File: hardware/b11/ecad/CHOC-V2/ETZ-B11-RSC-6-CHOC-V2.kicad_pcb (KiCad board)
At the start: 2 copper layers, 131.5 x 85.8 mm, 44 parts, among them SW1 Kailh_socket_PG1350, SW10 Kailh_socket_PG1350, SW11 Kailh_socket_PG1350, SW12 Kailh_socket_PG1350, SW13 Kailh_socket_PG1350, SW14 Kailh_socket_PG1350, SW15 Kailh_socket_PG1350, SW16 Kailh_socket_PG1350, SW17 Kailh_socket_PG1350, SW18 Kailh_socket_PG1350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

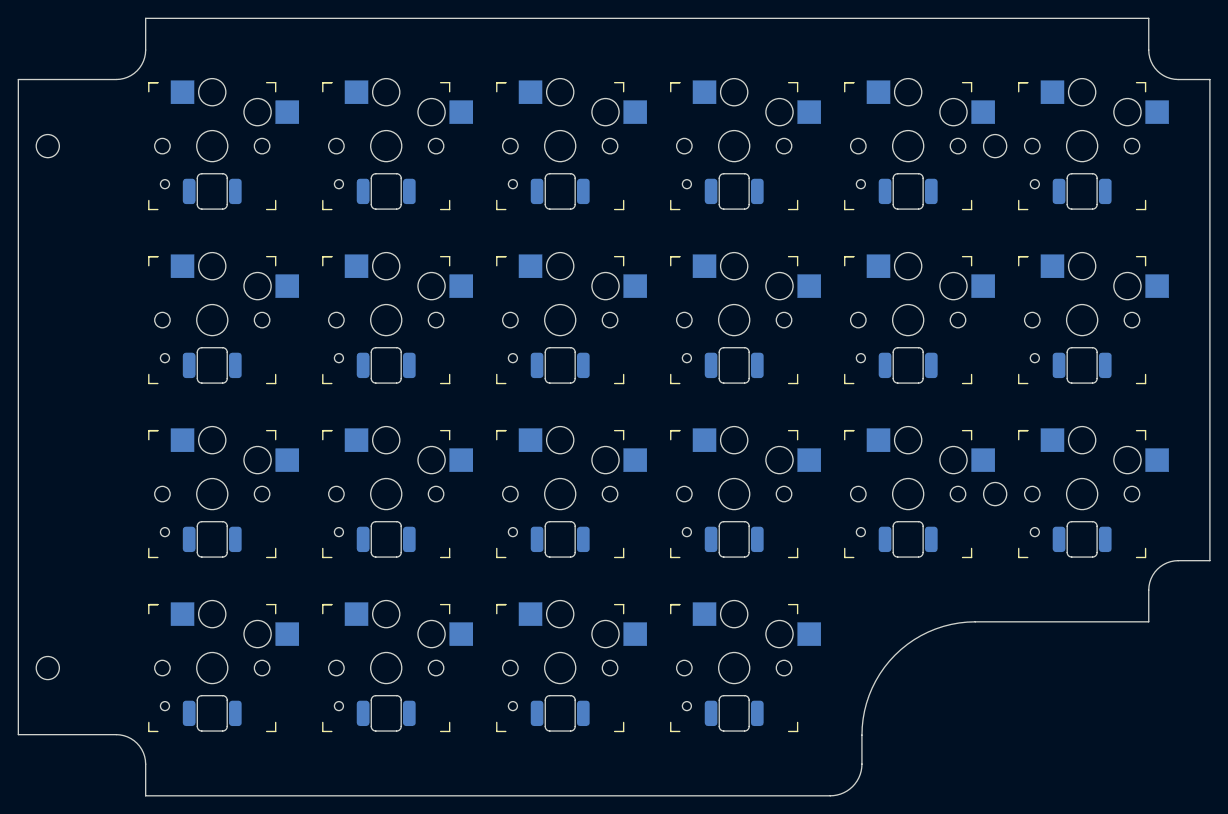
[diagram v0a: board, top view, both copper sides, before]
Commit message: Regenerate B11 PCBs after library cleanup [skip ci]
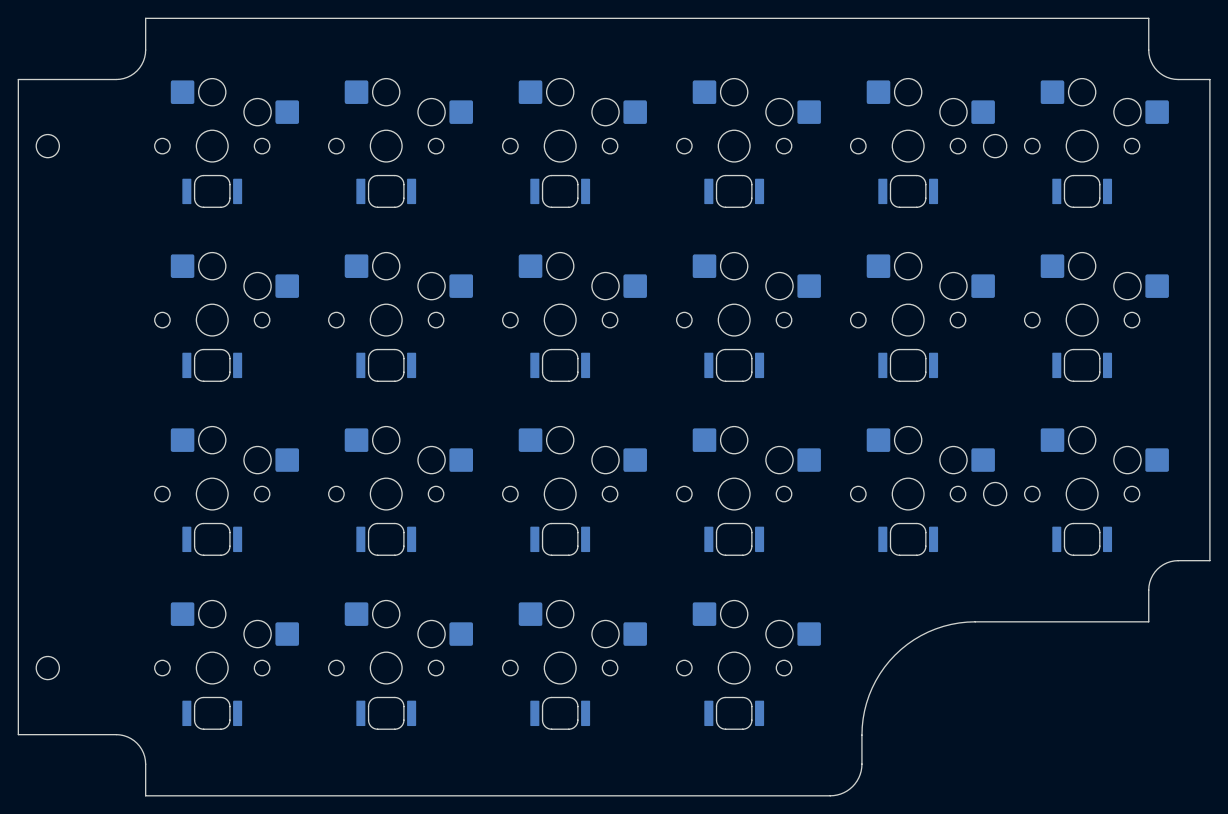
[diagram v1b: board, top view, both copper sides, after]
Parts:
- LED1, LED10, LED11, LED12, LED13, LED14, LED15, LED16, LED17, LED18, LED19, LED2, LED20, LED21, LED22, LED3, LED4, LED5, LED6, LED7, LED8, LED9: value LED_SMD_6028_BackMount -> 6028_LED; footprint LED_SMD_6028_BackMount -> 6028_LED; moved to F.Cu
- SW1, SW10, SW11, SW12, SW13, SW14, SW15, SW16, SW17, SW18, SW19, SW2, SW20, SW21, SW22, SW3, SW4, SW5, SW6, SW7, SW8, SW9: value Kailh_socket_PG1350 -> CPG135001S30; footprint Kailh_socket_PG1350 -> CPG135001S30
- turned SW1 to 0 degrees
- turned SW10 to 0 degrees
- turned SW11 to 0 degrees
- turned SW12 to 0 degrees
- turned SW13 to 0 degrees
- turned SW14 to 0 degrees
- turned SW15 to 0 degrees
- turned SW16 to 0 degrees
- turned SW17 to 0 degrees
- turned SW18 to 0 degrees
- turned SW19 to 0 degrees
- turned SW2 to 0 degrees
- turned SW20 to 0 degrees
- turned SW21 to 0 degrees
- turned SW22 to 0 degrees
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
